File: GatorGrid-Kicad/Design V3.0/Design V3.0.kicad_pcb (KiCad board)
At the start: 2 copper layers, 92 x 114 mm, 33 parts, among them J1 Battery-Connector, J2 Conn_01x20_Pin, J3 Conn_01x20_Pin, J4 Conn_01x20_Pin, J5 Conn_01x20_Pin, Q3 2N3904, Q4 2N3904, SW1 SW_SPST, U1 TP4056

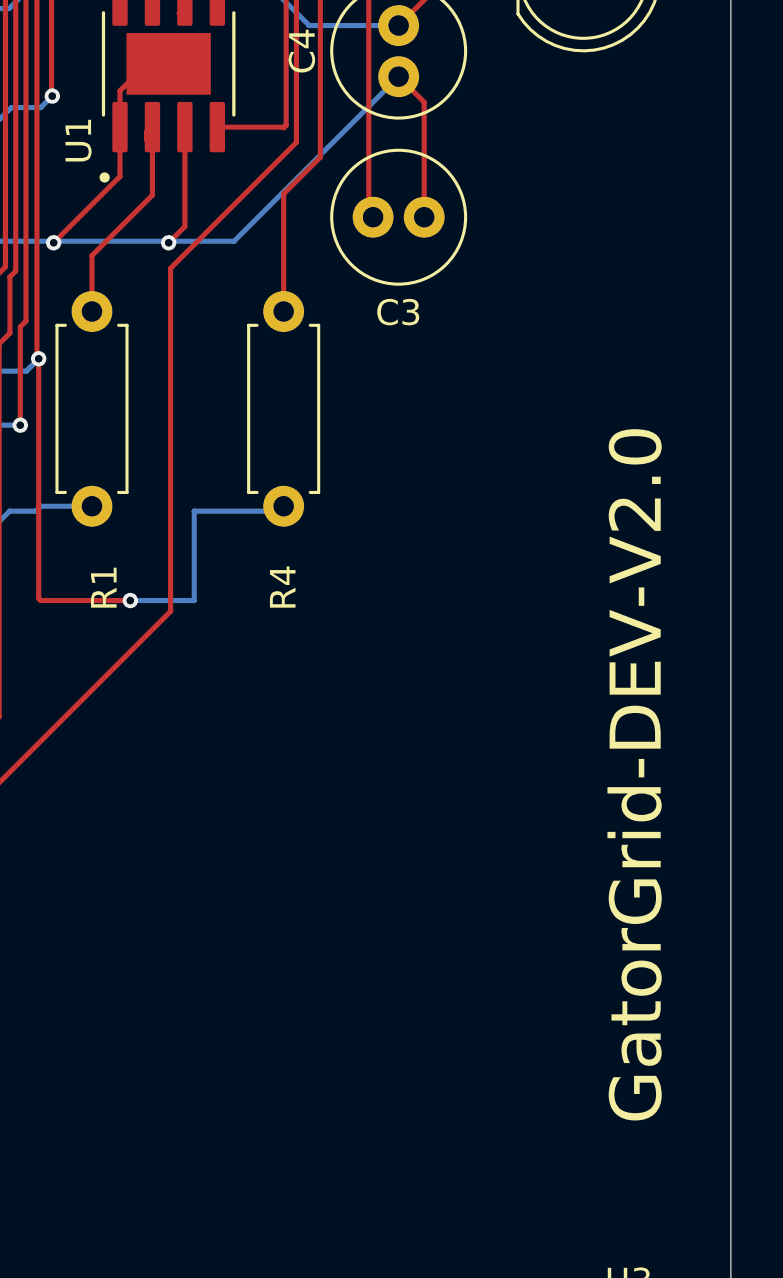
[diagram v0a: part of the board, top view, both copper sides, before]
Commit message: added an additional screw for an addition of a sensor PCB
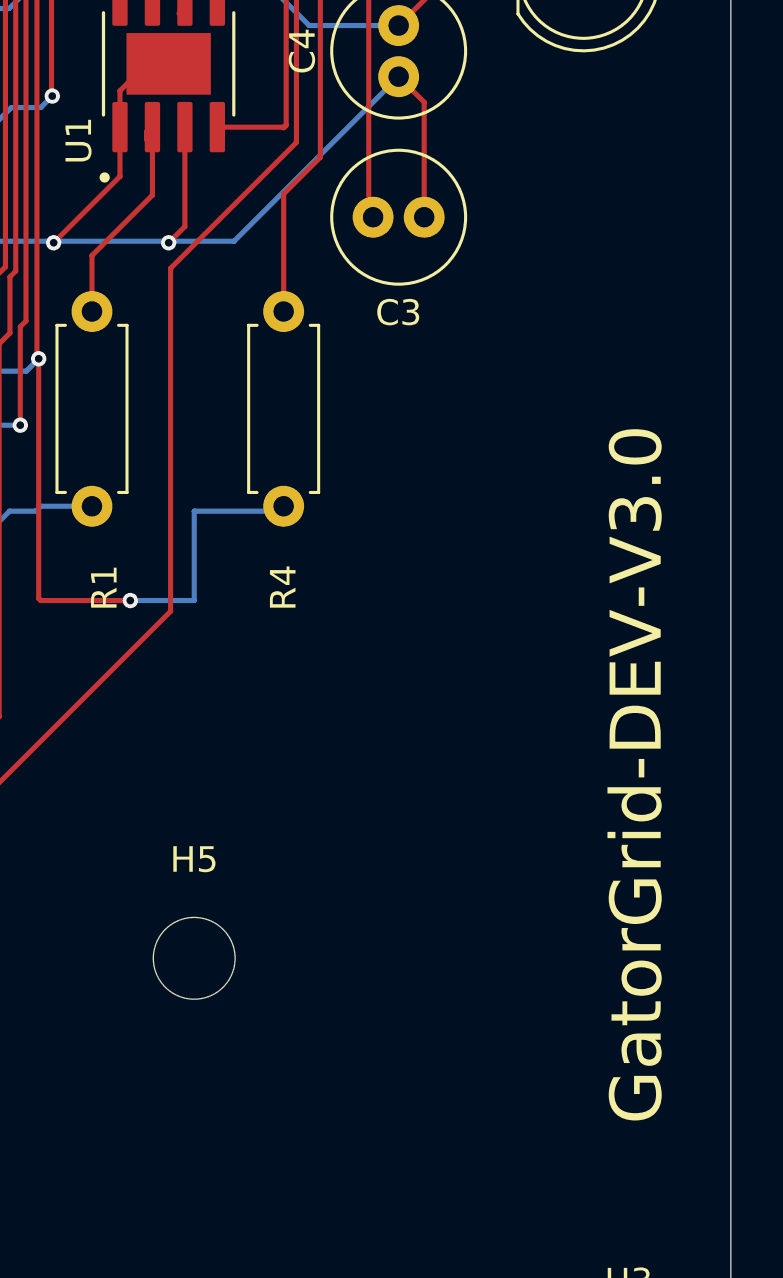
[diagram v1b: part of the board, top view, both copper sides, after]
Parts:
- added H5: MountingHole_3.2mm_M3_ISO7380, MountingHole:MountingHole_3.2mm_M3_ISO7380, F.Cu at (228.5, 121.0)
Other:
- board text added: "GatorGrid-DEV-V3.0"
- board text removed: "GatorGrid-DEV-V2.0"
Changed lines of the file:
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@@
 			(psa4output no)
 			(plot_black_and_white yes)
-			(plotinvisibletext no)
 			(sketchpadsonfab no)
 			(plotpadnumbers no)
@@
 		(embedded_fonts no)
 	)
+	(footprint "MountingHole:MountingHole_3.2mm_M3_ISO7380"
+		(layer "F.Cu")
+		(at 228.5 121)
+		(descr "Mounting Hole 3.2mm, no annular, M3, ISO7380")
+		(tags "mounting hole 3.2mm no annular m3 iso7380")
+		(property "Reference" "H5"
+			(at 0 -3.85 0)
+			(layer "F.SilkS")
+			(effects
+				(font
+					(size 1 1)
+					(thickness 0.15)
+				)
+			)
+		)
+		(property "Value" "MountingHole_3.2mm_M3_ISO7380"
+			(at 3 5.5 0)
+			(layer "F.Fab")
+			(effects
+				(font
+					(size 1 1)
+					(thickness 0.15)
+				)
+			)
+		)
+		(property "Datasheet" ""
+			(at 0 0 0)
+			(unlocked yes)
+			(layer "F.Fab")
+			(hide yes)
+			(effects
+				(font
+					(size 1.27 1.27)
+					(thickness 0.15)
+				)
+			)
+		)
+		(property "Description" ""
+			(at 0 0 0)
+			(unlocked yes)
+			(layer "F.Fab")
+			(hide yes)
+			(effects
+				(font
+					(size 1.27 1.27)
+					(thickness 0.15)
+				)
+			)
+		)
+		(attr exclude_from_pos_files exclude_from_bom)
+		(fp_circle
+			(center 0 0)
+			(end 2.85 0)
+			(stroke
+				(width 0.15)
+				(type solid)
+			)
+			(fill no)
+			(layer "Cmts.User")
+		)
+		(fp_circle
+			(center 0 0)
+			(end 3.1 0)
+			(stroke
+				(width 0.05)
+				(type solid)
+			)
+			(fill no)
+			(layer "F.CrtYd")
+		)
+		(fp_text user "${REFERENCE}"
+			(at 0 0 0)
+			(layer "F.Fab")
+			(effects
+				(font
+					(size 1 1)
+					(thickness 0.15)
+				)
+			)
+		)
+		(pad "" np_thru_hole circle
+			(at 0 0)
+			(size 3.2 3.2)
+			(drill 3.2)
+			(layers "*.Cu" "*.Mask")
+		)
+		(embedded_fonts no)
+	)
 	(footprint "LED_THT:LED_D5.0mm"
 		(layer "F.Cu")
@@
 		(layer "Edge.Cuts")
 	)
-	(gr_text "GatorGrid-DEV-V2.0"
+	(gr_text "GatorGrid-DEV-V3.0"
 		(at 247 127.5 90)
 		(layer "F.SilkS")

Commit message: Finalized V3.0
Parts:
- added J7: Conn_01x03, Connector_PinHeader_2.54mm:PinHeader_1x03_P2.54mm_Vertical, F.Cu at (226.0, 139.5)
- moved H5 4.50 mm to (233.0, 121.0)
- moved J1 3.50 mm to (241.6, 44.0), turned to 90 degrees
- moved D6 2.00 mm to (225.0, 31.2)
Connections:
- net A_GPIO22 renamed SENSOR_DATA
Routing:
- net A_3V3(OUT): track 123.2 -> 202.5 mm, vias 1 -> 2
- net SENSOR_DATA: track 59.7 -> 124.1 mm, vias 0 -> 2
- net GND: track 595.9 -> 632.9 mm, vias 4 -> 1
- net B_GPIO26: track 85.7 -> 60.5 mm, vias 1 -> 0
- net B_RUN: track 58.8 -> 80.7 mm, vias 1 -> 4
- net TX-RX: track 133.2 -> 149.4 mm
- net A_ADC_VREF: track 74.3 -> 59.9 mm, vias 1 -> 0
- net RX-TX: track 132.6 -> 146.2 mm
- net A_GPIO3: track 72.6 -> 61.5 mm, vias 0 -> 1
- net A_GPIO21: track 59.5 -> 69.6 mm, vias 1 -> 3
- net B_GPIO8: track 68.2 -> 58.2 mm
- net B_GPIO3: track 69.7 -> 60.2 mm
- net A_GPIO27: track 67.7 -> 59.5 mm
- net A_GPIO4: track 58.9 -> 67.0 mm, vias 1 -> 3
- net UART_RX: track 132.0 -> 124.2 mm
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
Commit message: Finished V3
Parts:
- A1: value A-RPICO-AP -> A-RPICO-STA
- A2: value B-RPICO-STA -> B-RPICO-AP
- J7: footprint Connector_PinHeader_2.54mm:PinHeader_1x03_P2.54mm_Vertical -> Connector_JST:JST_XH_S3B-XH-A_1x03_P2.50mm_Horizontal
- moved H5 10.0 mm to (233.0, 111.0)
- moved J7 9.01 mm to (227.0, 130.6), turned to 0 degrees
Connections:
- J7 pad 1: SENSOR_DATA -> A_3V3(OUT)
- J7 pad 2: A_3V3(OUT) -> SENSOR_DATA
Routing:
- net A_3V3(OUT): track 202.5 -> 193.5 mm
- net SENSOR_DATA: track 124.1 -> 115.5 mm, vias 2 -> 3
- net GND: track 632.9 -> 635.6 mm
